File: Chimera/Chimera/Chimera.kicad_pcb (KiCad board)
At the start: 4 copper layers, 72 x 57.9 mm, 117 parts, among them IC1 AP7375-50W5-7, J1 Fork 1, J10 DM3CS-SF, J11 Reciver, J2 Fork 2, J3 Flamethrower, J4 Therm 1, J5 Therm 2, J6 Therm 3, J7 Therm 4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

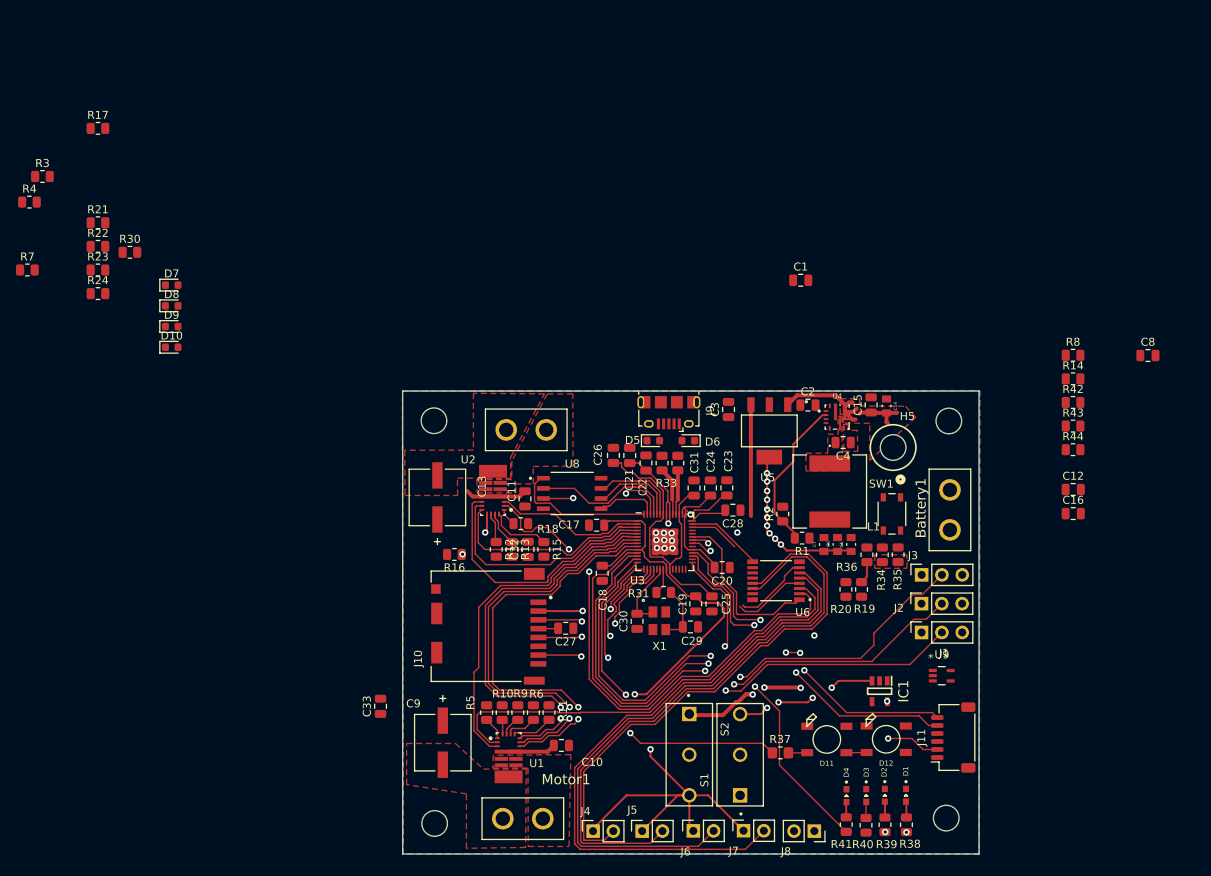
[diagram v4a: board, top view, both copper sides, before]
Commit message: Finalized MUX and thermistor wiring, Need to revise Buck and add Opamp surronding circuitry
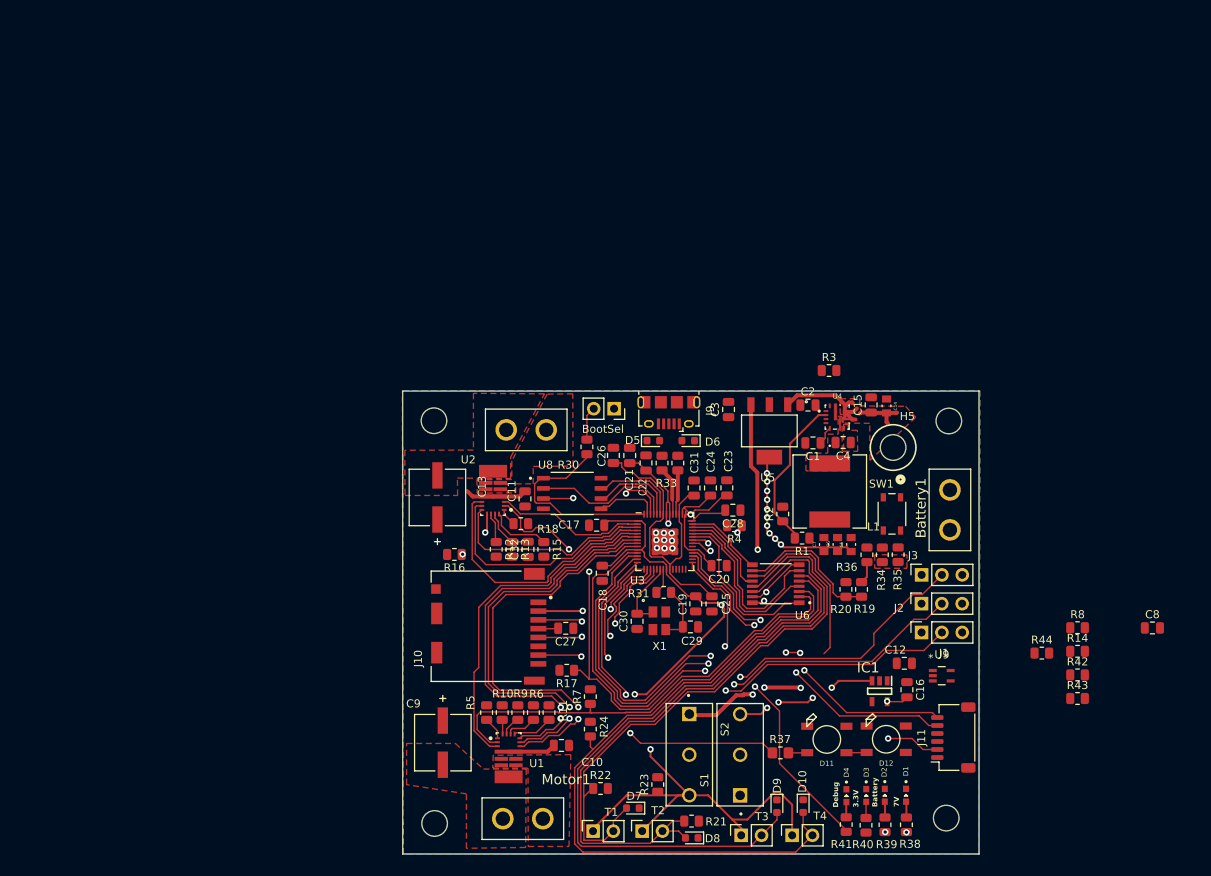
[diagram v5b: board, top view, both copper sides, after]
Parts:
- removed C33: .1uF, Capacitor_SMD:C_0805_2012Metric
- moved R21 105.4 mm to (108.0, 115.5)
- moved R3 101.3 mm to (125.2, 59.1)
- moved D10 97.6 mm to (121.9, 113.6), turned to -90 degrees
- moved R4 97.0 mm to (113.3, 78.5), turned to 180 degrees
- moved D9 96.5 mm to (118.7, 113.6), turned to -90 degrees
- moved R23 95.0 mm to (103.8, 110.9), turned to 90 degrees
- moved D8 93.0 mm to (108.0, 117.6), turned to 180 degrees
- moved R22 92.4 mm to (96.6, 111.4)
- moved R17 89.6 mm to (92.4, 96.6), turned to 180 degrees
- moved R7 88.3 mm to (95.3, 99.9), turned to 90 degrees
- moved D7 87.2 mm to (100.6, 113.8), turned to 180 degrees
- moved R24 82.2 mm to (95.3, 104.0), turned to 90 degrees
- moved R30 62.1 mm to (94.9, 68.7), turned to -90 degrees
- moved BootSel 58.4 mm to (98.3, 63.9)
- moved R43 34.1 mm to (156.2, 100.2)
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- renumbered J8 to BootSel, J4 to T1, J5 to T2, J6 to T3, J7 to T4
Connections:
- U3 pad 38: Therm3/4 -> IPROPI1/2
- U3 pad 39: Therm1/2 -> Therm3/4
- U3 pad 40: IPROPI1/2 -> Therm1/2
- U6 pad 10: Current_Sense -> /V_Bat_Mon
- U6 pad 11: /V_Bat_Mon -> Current_Sense
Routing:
- net Current_Sense: track 0.00 -> 22.2 mm
- net /V_Bat_Mon: track 0.00 -> 18.5 mm
- net Net-(U5-OUTPUT): track 37.3 -> 55.5 mm
- net +3.3V: track 142.0 -> 158.5 mm, vias 4 -> 6
- net Therm3/4: track 9.56 -> 23.4 mm
- net Therm1/2: track 0.00 -> 11.8 mm
- net /Therm4: track 78.4 -> 89.5 mm
- net /Therm3: track 72.1 -> 81.4 mm
- net GND: track 20.9 -> 28.6 mm, vias 19 -> 20
- net /MCU/QSPI_SS: track 17.9 -> 24.8 mm
- net IPROPI1/2: track 15.5 -> 21.9 mm
- net /Therm2: track 74.7 -> 80.9 mm
- net /Therm1: track 68.3 -> 73.2 mm
- net Net-(J8-Pin_2): track 0.00 -> 4.21 mm
- net IPROPI2: track 66.3 -> 69.1 mm
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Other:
- board text added: "3.3V"
- board text added: "7V"
- board text added: "Battery"
- board text added: "Debug"

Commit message: Final Board and BOM
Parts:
- removed H1: MountingHole, MountingHole:MountingHole_3.2mm_M3
- added H6: MountingHole, MountingHole:MountingHole_3.2mm_M3, F.Cu at (75.8, 65.5)
- Motor 2: renamed from U2
- R3: moved to B.Cu
- Switch: renamed from H5; footprint MountingHole:MountingHole_3.2mm_M3 -> chimera:screwswitch
- moved H4 64.0 mm to (139.8, 65.5)
- moved C8 30.9 mm to (136.2, 100.8), turned to 90 degrees
- moved R14 20.8 mm to (135.5, 95.6), turned to 90 degrees
- moved R43 16.8 mm to (139.5, 100.5)
- moved R23 16.5 mm to (120.0, 113.5)
- moved R8 14.4 mm to (142.6, 96.0), turned to -90 degrees
- moved R42 13.8 mm to (142.6, 99.5), turned to 90 degrees
- moved R44 13.2 mm to (138.6, 94.8)
- moved R3 4.48 mm to (122.8, 63.0), turned to 180 degrees
- moved C12 3.36 mm to (131.2, 96.0), turned to 0 degrees
- moved C14 2.21 mm to (130.5, 64.8), turned to 180 degrees
- moved C16 2.10 mm to (132.8, 99.2)
- moved IC1 1.68 mm to (129.8, 99.3)
- moved J11 1.43 mm to (140.6, 106.5)
- moved T3 1.16 mm to (113.0, 117.2)
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- renumbered S2 to 3.3V, S1 to 7V, Battery1 to Battery, BootSel to J8
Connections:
- D6 pad 2: Net-(D5-A2) -> Net-(D6-A2)
- J9 pad 2: Net-(D5-A2) -> Net-(D6-A2)
- J9 pad 3: Net-(J9-D+) -> Net-(D5-A2)
- R18 pad 1: +3V3 -> +3.3V
- R32 pad 1: Net-(J9-D+) -> Net-(D5-A2)
- R33 pad 2: Net-(D5-A2) -> Net-(D6-A2)
- R5 pad 1: +3V3 -> +3.3V
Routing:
- net GND: track 28.6 -> 177.0 mm, vias 20 -> 81
- net +3.3V: track 158.5 -> 274.3 mm, vias 6 -> 14
- net PG: track 7.07 -> 34.6 mm, vias 2 -> 3
- net Enable: track 2.13 -> 28.6 mm, vias 1 -> 2
- net Current_Sense: track 22.2 -> 43.9 mm, vias 0 -> 2
- net Servo_Current_Sense: track 0.00 -> 11.8 mm
- net /MCU/OpF-: track 0.00 -> 7.50 mm
- net +BATT: track 36.3 -> 43.1 mm, vias 1 -> 15
- net Net-(U9-+): track 0.00 -> 6.25 mm
- net Net-(R35-Pad2): track 0.00 -> 4.39 mm
- net Net-(D5-A2): track 0.00 -> 4.34 mm
- net Net-(D6-A2): track 0.00 -> 4.18 mm
- net Net-(U5-OUTPUT): track 55.5 -> 58.2 mm
- net /MCU/Transmitter-MCU_TX: track 41.9 -> 43.8 mm
- net Net-(R34-Pad1): track 0.00 -> 1.92 mm
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- added copper zone on F.Cu, net +7.5V
